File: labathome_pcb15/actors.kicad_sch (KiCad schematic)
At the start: 39 parts, among them J18 K1, J24 K1, J26 Servos, J7 FAN5V, J8 3V GN RGB 5V, K1 G6K-2, Q1 BC817, Q2 IRLML6344, Q3 MJD31C, Q4 BC817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

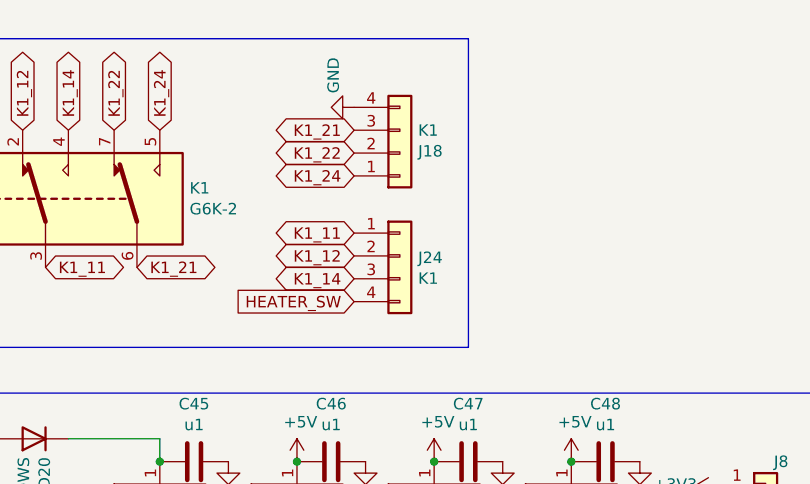
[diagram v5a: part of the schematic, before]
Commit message: Added Stepper Motors (initial)
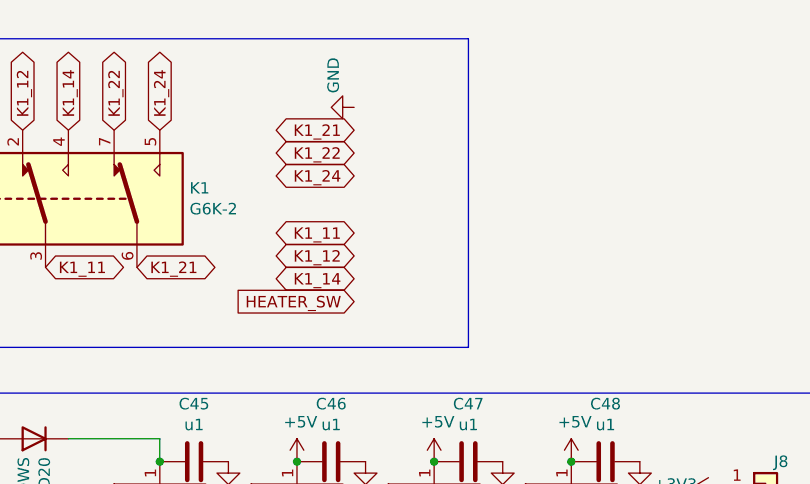
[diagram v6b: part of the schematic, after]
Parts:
- removed J18, J24: K1, liebler_CONN:PhoenixContact_MC_1,5_4-G-3.5_1x04_P3.50mm_Horizontal_smallerCourtyard, symbol Connector_Generic:Conn_01x04
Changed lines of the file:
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@@
-	)
-	(symbol
-		(lib_id "Connector_Generic:Conn_01x04")
-		(at 139.7 39.37 0)
-		(unit 1)
-		(exclude_from_sim no)
-		(in_bom yes)
-		(on_board yes)
-		(dnp no)
-		(property "Reference" "J24"
-			(at 141.732 39.5732 0)
-			(effects
-				(font
-					(size 1.27 1.27)
-				)
-				(justify left)
-			)
-		)
-		(property "Value" "K1"
-			(at 141.732 41.8846 0)
-			(effects
-				(font
-					(size 1.27 1.27)
-				)
-				(justify left)
-			)
-		)
-		(property "Footprint" "liebler_CONN:PhoenixContact_MC_1,5_4-G-3.5_1x04_P3.50mm_Horizontal_smallerCourtyard"
-			(at 139.7 39.37 0)
-			(effects
-				(font
-					(size 1.27 1.27)
-				)
-				(hide yes)
-			)
-		)
-		(property "Datasheet" "~"
-			(at 139.7 39.37 0)
-			(effects
-				(font
-					(size 1.27 1.27)
-				)
-				(hide yes)
-			)
-		)
-		(property "Description" ""
-			(at 139.7 39.37 0)
-			(effects
-				(font
-					(size 1.27 1.27)
-				)
-				(hide yes)
-			)
-		)
-		(pin "1"
-		)
-		(pin "2"
-		)
-		(pin "3"
-		)
-		(pin "4"
-		)
-		(instances
-			(project "labathome_pcb15"
-				(path "/e4d6926a-1a8b-424d-97c4-66b6ad87e4ac/7cc4a29d-fb70-4313-b60c-aaf23d93fc45"
-					(reference "J24")
-					(unit 1)
-				)
-			)
-		)
 	)
 	(symbol
@@
 					(unit 1)
 				)
-			)
-		)
-	)
-	(symbol
-		(lib_id "Connector_Generic:Conn_01x04")
-		(at 139.7 27.94 0)
-		(mirror x)
-		(unit 1)
-		(exclude_from_sim no)
-		(in_bom yes)
-		(on_board yes)
-		(dnp no)
-		(property "Reference" "J18"
-			(at 141.732 27.7368 0)
-			(effects
-				(font
-					(size 1.27 1.27)
-				)
-				(justify left)
-			)
-		)
-		(property "Value" "K1"
-			(at 141.732 25.4254 0)
-			(effects
-				(font
-					(size 1.27 1.27)
-				)
-				(justify left)
-			)
-		)
-		(property "Footprint" "liebler_CONN:PhoenixContact_MC_1,5_4-G-3.5_1x04_P3.50mm_Horizontal_smallerCourtyard"
-			(at 139.7 27.94 0)
-			(effects
-				(font
-					(size 1.27 1.27)
-				)
-				(hide yes)
-			)
-		)
-		(property "Datasheet" "~"
-			(at 139.7 27.94 0)
-			(effects
-				(font
-					(size 1.27 1.27)
-				)
-				(hide yes)
-			)
-		)
-		(property "Description" ""
-			(at 139.7 27.94 0)
-			(effects
-				(font
-					(size 1.27 1.27)
-				)
-				(hide yes)
-			)
-		)
-		(pin "1"
-		)
-		(pin "2"
-		)
-		(pin "3"
-		)
-		(pin "4"
-		)
-		(instances
-			(project "labathome_pcb15"
-				(path "/e4d6926a-1a8b-424d-97c4-66b6ad87e4ac/7cc4a29d-fb70-4313-b60c-aaf23d93fc45"
-					(reference "J18")
-					(unit 1)
-				)

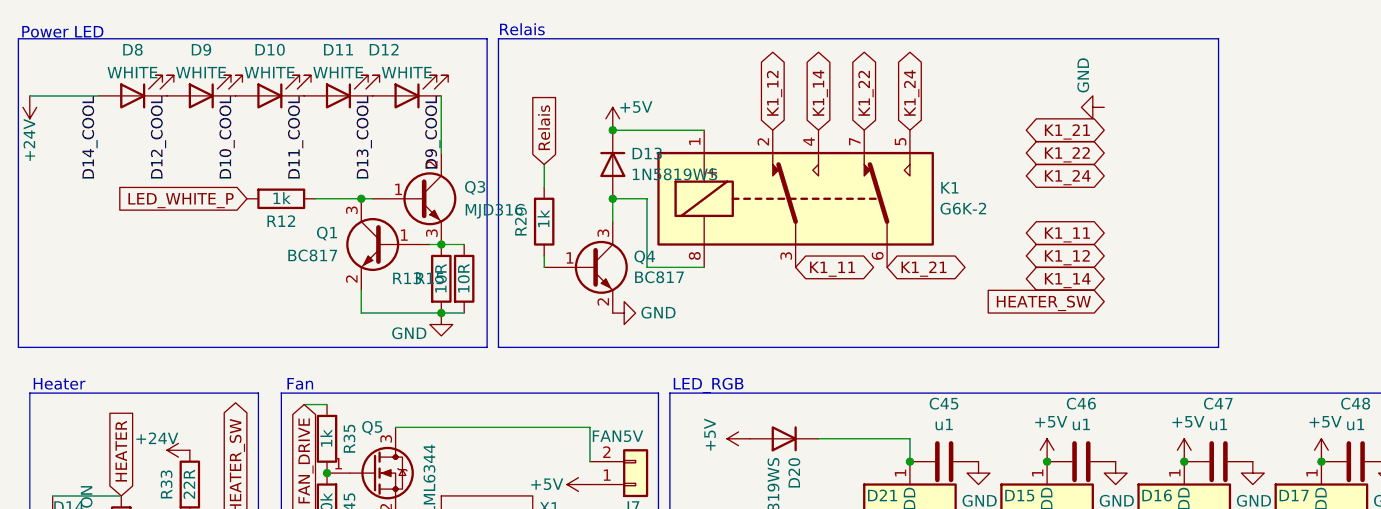
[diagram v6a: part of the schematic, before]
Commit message: Added stepper, no DRC errors, not yet optimized
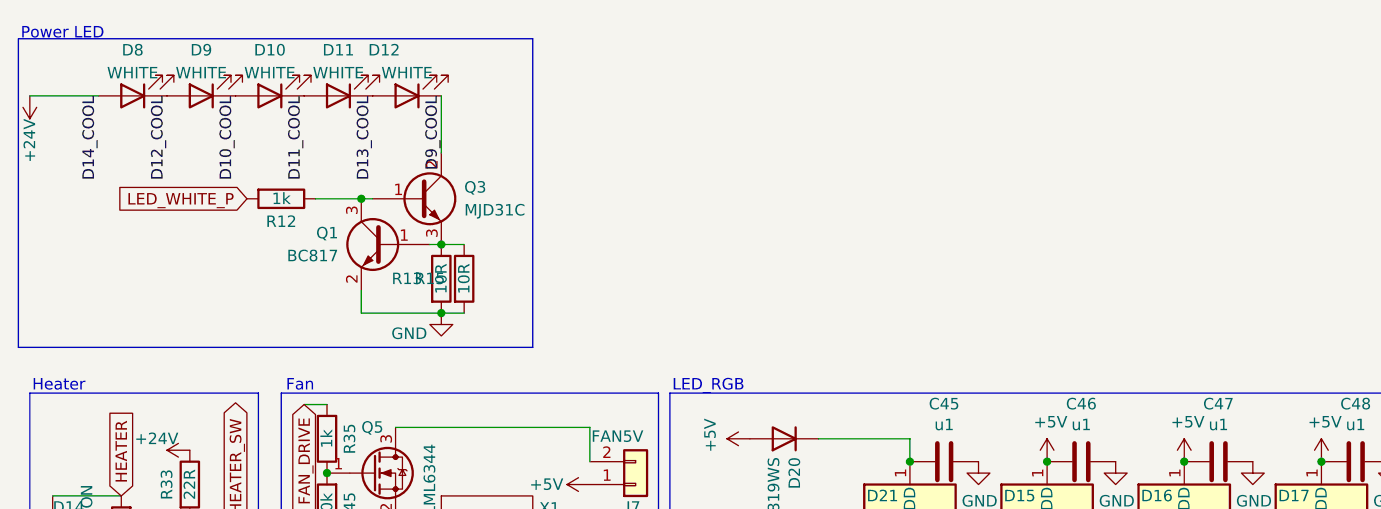
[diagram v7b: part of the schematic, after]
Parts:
- removed D13: 1N5819WS, Diode_SMD:D_SOD-323, symbol Device:D
- removed K1: G6K-2, Relay_SMD:Relay_DPDT_Omron_G6K-2F-Y, symbol Relay:G6K-2
- removed Q4: BC817, Package_TO_SOT_SMD:SOT-23, symbol Transistor_BJT:BC817
- removed R29: 1k, Resistor_SMD:R_0402_1005Metric, symbol Device:R
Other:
- note removed: "Relais"
